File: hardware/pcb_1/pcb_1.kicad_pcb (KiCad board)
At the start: 2 copper layers, 50 x 50 mm, 5 parts, among them J1 Connector, USB-TYPE-C-16P

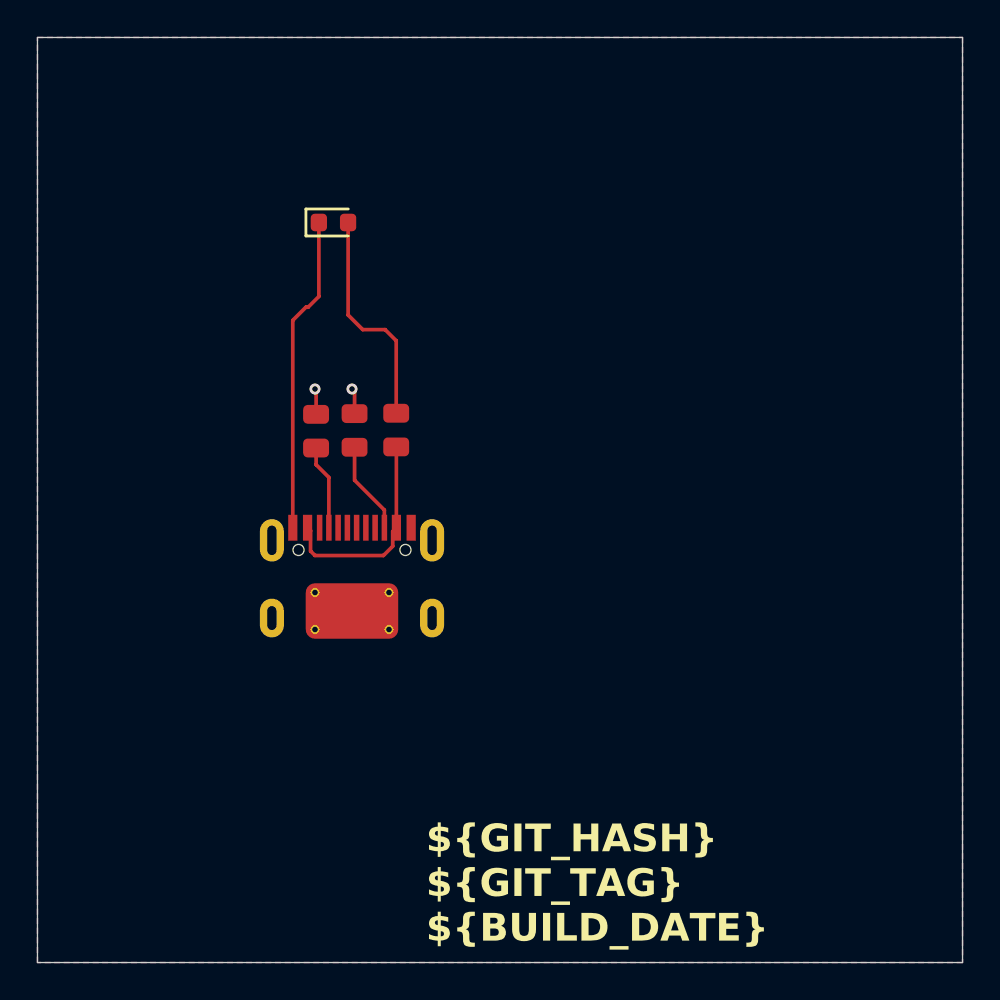
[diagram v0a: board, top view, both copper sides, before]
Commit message: Resize pcb_1 board outline and move components
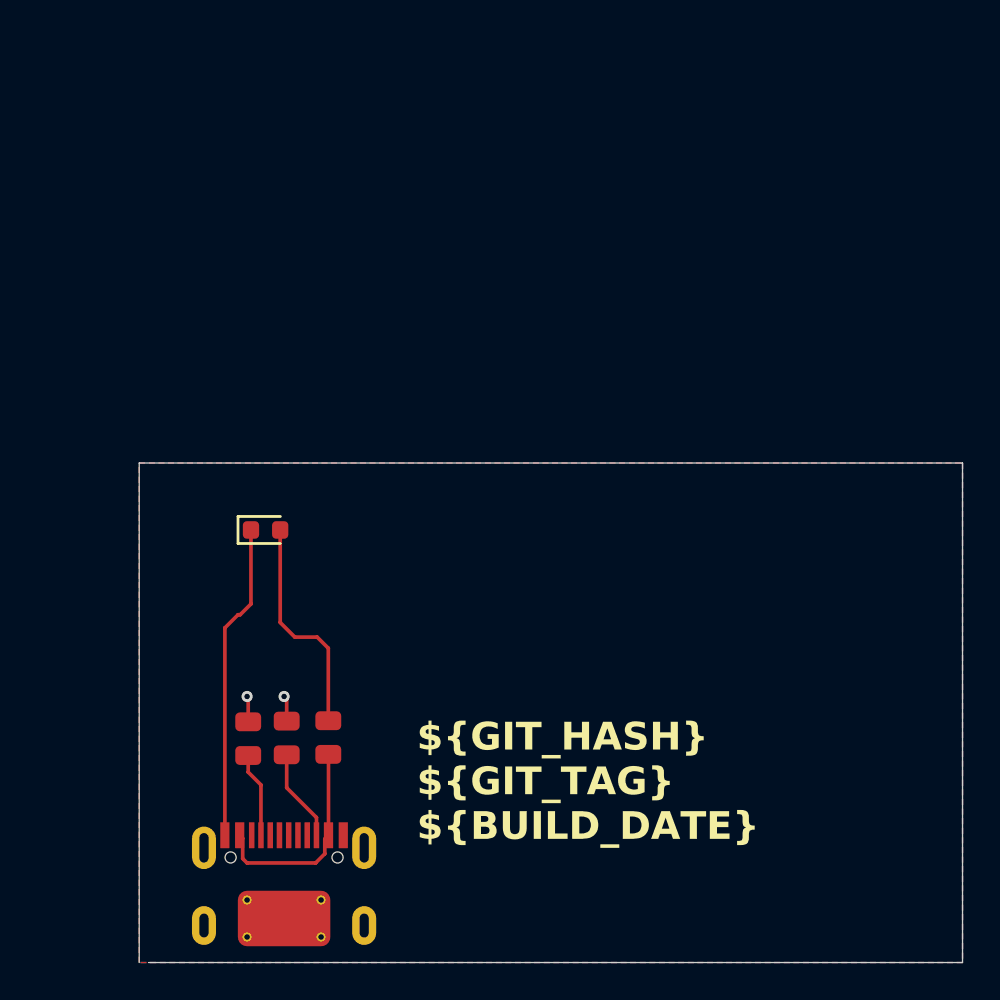
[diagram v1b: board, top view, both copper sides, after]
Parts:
- moved D1 17.0 mm to (112.3, 76.6)
- moved J1 17.0 mm to (113.3, 95.6)
- moved R1 17.0 mm to (115.7, 87.8)
- moved R2 17.0 mm to (113.5, 87.9)
- moved R3 17.0 mm to (111.4, 87.9)
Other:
- board size 50 x 50 mm -> 44.5 x 27 mm
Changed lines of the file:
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@@
 	(footprint "PCM_JLCPCB:R_0805"
 		(layer "F.Cu")
-		(at 119.39 71.22 90)
+		(at 115.72 87.84 90)
 		(descr "Resistor SMD 0805 (2012 Metric), square (rectangular) end terminal, IPC_7351 nominal, (Body size source: IPC-SM-782 page 72, https://www.pcb-3d.com/wordpress/wp-content/uploads/ipc-sm-782a_amendment_1_and_2.pdf), generated with kicad-footprint-generator")
 		(tags "resistor")
@@
 	(footprint "PCM_JLCPCB:R_0805"
 		(layer "F.Cu")
-		(at 117.14 71.24 90)
+		(at 113.47 87.86 90)
 		(descr "Resistor SMD 0805 (2012 Metric), square (rectangular) end terminal, IPC_7351 nominal, (Body size source: IPC-SM-782 page 72, https://www.pcb-3d.com/wordpress/wp-content/uploads/ipc-sm-782a_amendment_1_and_2.pdf), generated with kicad-footprint-generator")
 		(tags "resistor")
@@
 	(footprint "PCM_JLCPCB:TYPE-C-SMD_HX-TYPE-C-16PIN"
 		(layer "F.Cu")
-		(at 117 79)
+		(at 113.33 95.62)
 		(descr "TYPE-C-SMD_HX-TYPE-C-16PIN footprint")
 		(tags "TYPE-C-SMD_HX-TYPE-C-16PIN footprint C2927039")
@@
 			(at 0 7.08 0)
 			(layer "F.Fab")
+			(hide yes)
 			(effects
 				(font
@@
 		)
 		(fp_text user "REF**"
-			(at 0 9.08 0)
+			(at 0 1.0375 0)
+			(unlocked yes)
 			(layer "F.Fab")
 			(effects
@@
 	(footprint "PCM_JLCPCB:D_0603"
 		(layer "F.Cu")
-		(at 116 60)
+		(at 112.33 76.62)
 		(descr "LED SMD 0603 (1608 Metric), square (rectangular) end terminal, IPC_7351 nominal, (Body size source: http://www.tortai-tech.com/upload/download/2011102023233369053.pdf), generated with kicad-footprint-generator")
 		(tags "LED")
@@
 	(footprint "PCM_JLCPCB:R_0805"
 		(layer "F.Cu")
-		(at 115.06 71.28 90)
+		(at 111.39 87.9 90)
 		(descr "Resistor SMD 0805 (2012 Metric), square (rectangular) end terminal, IPC_7351 nominal, (Body size source: IPC-SM-782 page 72, https://www.pcb-3d.com/wordpress/wp-content/uploads/ipc-sm-782a_amendment_1_and_2.pdf), generated with kicad-footprint-generator")
 		(tags "resistor")
@@
 	)
 	(gr_line
-		(start 100 50)
-		(end 150 50)
+		(start 105.5 73)
+		(end 150 73)
 		(stroke
 			(width 0.05)
@@
 	)
 	(gr_line
-		(start 150 50)
+		(start 150 73)
 		(end 150 100)
 		(stroke
@@
 	)
 	(gr_line
-		(start 100 100)
-		(end 100 50)
+		(start 105.5 100)
+		(end 105.5 73)
 		(stroke
 			(width 0.05)
@@
 	(gr_line
 		(start 150 100)
-		(end 100 100)
+		(end 106 100)
 		(stroke
 			(width 0.05)
@@
 	)
 	(gr_text "${GIT_HASH}\n${GIT_TAG}\n${BUILD_DATE}"
-		(at 121 99 0)
+		(at 120.5 93.5 0)
 		(layer "F.SilkS")
 		(effects
@@
 	)
 	(segment
-		(start 119.39 70.31)
-		(end 119.39 66.39)
+		(start 115.72 86.93)
+		(end 115.72 83.01)
 		(width 0.2)
 		(layer "F.Cu")
@@
 	)
 	(segment
-		(start 118.79 65.79)
-		(end 117.58 65.79)
+		(start 115.12 82.41)
+		(end 113.91 82.41)
 		(width 0.2)
 		(layer "F.Cu")
@@
 	)
 	(segment
-		(start 119.39 66.39)
-		(end 118.79 65.79)
+		(start 115.72 83.01)
+		(end 115.12 82.41)
 		(width 0.2)
 		(layer "F.Cu")
@@
 	)
 	(segment
-		(start 116.79 65)
-		(end 116.79 60)
+		(start 113.12 81.62)
+		(end 113.12 76.62)
 		(width 0.2)
 		(layer "F.Cu")
@@
 	)
 	(segment
-		(start 117.58 65.79)
-		(end 116.79 65)
+		(start 113.91 82.41)
+		(end 113.12 81.62)
 		(width 0.2)
 		(layer "F.Cu")
@@
 	)
 	(segment
-		(start 117.14 70.33)
-		(end 117.14 69.14)
+		(start 113.47 86.95)
+		(end 113.47 85.76)
 		(width 0.2)
 		(layer "F.Cu")
@@
 	)
 	(segment
-		(start 114.63 64.58)
-		(end 115.21 64)
+		(start 110.96 81.2)
+		(end 111.54 80.62)
 		(width 0.2)
 		(layer "F.Cu")
@@
 	)
 	(segment
-		(start 115.06 70.37)
-		(end 115.06 69.06)
+		(start 111.39 86.99)
+		(end 111.39 85.68)
 		(width 0.2)
 		(layer "F.Cu")
@@
 	)
 	(segment
-		(start 115.21 64)
-		(end 115.21 60)
+		(start 111.54 80.62)
+		(end 111.54 76.62)
 		(width 0.2)
 		(layer "F.Cu")
@@
 	)
 	(segment
-		(start 113.8 65.29)
-		(end 114.51 64.58)
+		(start 110.13 81.91)
+		(end 110.84 81.2)
 		(width 0.2)
 		(layer "F.Cu")
@@
 	)
 	(segment
-		(start 113.8 76.5)
-		(end 113.8 65.29)
+		(start 110.13 93.12)
+		(end 110.13 81.91)
 		(width 0.2)
 		(layer "F.Cu")
@@
 	)
 	(segment
-		(start 114.51 64.58)
-		(end 114.63 64.58)
+		(start 110.84 81.2)
+		(end 110.96 81.2)
 		(width 0.2)
 		(layer "F.Cu")
@@
 	)
 	(segment
-		(start 115.06 69.06)
-		(end 115 69)
+		(start 111.39 85.68)
+		(end 111.33 85.62)
 		(width 0.2)
 		(layer "F.Cu")
@@
 	)
 	(segment
-		(start 117.14 69.14)
-		(end 117 69)
+		(start 113.47 85.76)
+		(end 113.33 85.62)
 		(width 0.2)
 		(layer "F.Cu")
@@
 	)
 	(via
-		(at 115 69)
+		(at 111.33 85.62)
 		(size 0.6)
 		(drill 0.3)
@@
 	)
 	(via
-		(at 117 69)
+		(at 113.33 85.62)
 		(size 0.6)
 		(drill 0.3)
@@
 	)
 	(segment
-		(start 114.761 76.661)
-		(end 114.761 77.761)
+		(start 111.091 93.281)
+		(end 111.091 94.381)
 		(width 0.2)
 		(layer "F.Cu")
@@
 	)
 	(segment
-		(start 119.4 76.5)
-		(end 119.4 72.14)
+		(start 115.73 93.12)
+		(end 115.73 88.76)
 		(width 0.2)
 		(layer "F.Cu")
@@
 	)
 	(segment
-		(start 119.201 77.501)
-		(end 119.201 76.699)
+		(start 115.531 94.121)
+		(end 115.531 93.319)
 		(width 0.2)
 		(layer "F.Cu")
@@
 	)
 	(segment
-		(start 119.201 76.699)
-		(end 119.4 76.5)
+		(start 115.531 93.319)
+		(end 115.73 93.12)
 		(width 0.2)
 		(layer "F.Cu")
@@
 	)
 	(segment
-		(start 115 78)
-		(end 118.702 78)
+		(start 111.33 94.62)
+		(end 115.032 94.62)
 		(width 0.2)
 		(layer "F.Cu")
@@
 	)
 	(segment
-		(start 114.6 76.5)
-		(end 114.761 76.661)
+		(start 110.93 93.12)
+		(end 111.091 93.281)
 		(width 0.2)
 		(layer "F.Cu")
@@
 	)
 	(segment
-		(start 119.4 72.14)
-		(end 119.39 72.13)
+		(start 115.73 88.76)
+		(end 115.72 88.75)
 		(width 0.2)
 		(layer "F.Cu")
@@
 	)
 	(segment
-		(start 114.761 77.761)
-		(end 115 78)
+		(start 111.091 94.381)
+		(end 111.33 94.62)
 		(width 0.2)
 		(layer "F.Cu")
@@
 	)
 	(segment
-		(start 118.702 78)
-		(end 119.201 77.501)
+		(start 115.032 94.62)
+		(end 115.531 94.121)
 		(width 0.2)
 		(layer "F.Cu")
@@
 	)
 	(segment
-		(start 118.75 75.54)
-		(end 117.14 73.93)
+		(start 115.08 92.16)
+		(end 113.47 90.55)
 		(width 0.2)
 		(layer "F.Cu")
@@
 	)
 	(segment
-		(start 117.14 73.93)
-		(end 117.14 72.15)
+		(start 113.47 90.55)
+		(end 113.47 88.77)
 		(width 0.2)
 		(layer "F.Cu")
@@
 	)
 	(segment
-		(start 118.75 76.5)
-		(end 118.75 75.54)
+		(start 115.08 93.12)
+		(end 115.08 92.16)
 		(width 0.2)
 		(layer "F.Cu")
@@
 	)
 	(segment
-		(start 115.75 76.5)
-		(end 115.75 73.78)
+		(start 112.08 93.12)
+		(end 112.08 90.4)
 		(width 0.2)
 		(layer "F.Cu")
@@
 	)
 	(segment
-		(start 115.06 73.09)
-		(end 115.06 72.19)
+		(start 111.39 89.71)
+		(end 111.39 88.81)
 		(width 0.2)
 		(layer "F.Cu")
@@
 	)
 	(segment
-		(start 115.75 73.78)
-		(end 115.06 73.09)
+		(start 112.08 90.4)
+		(end 111.39 89.71)
 		(width 0.2)
 		(layer "F.Cu")
@@
 		(min_thickness 0.25)
 		(filled_areas_thickness no)
-		(fill yes
+		(fill
 			(thermal_gap 0.5)
 			(thermal_bridge_width 0.5)
@@
 		(polygon
 			(pts
-				(xy 100 50) (xy 150 50) (xy 150 100) (xy 100 100)
+				(xy 105.5 73) (xy 150 73) (xy 150 100) (xy 105.5 100)
 			)
 		)
@@
 		(min_thickness 0.25)
 		(filled_areas_thickness no)
-		(fill yes
+		(fill
 			(thermal_gap 0.5)
 			(thermal_bridge_width 0.5)
@@
 		(polygon
 			(pts
-				(xy 100 50) (xy 150 50) (xy 150 100) (xy 100 100)
-			)
-		)
+				(xy 105.5 73) (xy 150 73) (xy 150 100) (xy 105.5 100)
+			)
+		)
